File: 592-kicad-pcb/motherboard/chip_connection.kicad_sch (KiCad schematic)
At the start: 28 parts, among them J3 DF40C-40DP-0.4V(51), J4 DF40C-40DP-0.4V(51), J5 Conn_01x16, J6 Conn_01x16, J7 Conn_01x16

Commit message: finalize termination
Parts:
- removed J5, J6, J7: Conn_01x16, Connector_PinHeader_2.54mm:PinHeader_1x16_P2.54mm_Vertical, symbol Connector_Generic:Conn_01x16
- removed R10, R14, R15, R16, R17, R19, R20, R8, R9: 10k, Resistor_SMD:R_0603_1608Metric, symbol Device:R_Small
- removed R74, R75, R76, R77: 0, Resistor_SMD:R_0402_1005Metric, symbol Device:R_Small
- added C50: 100n, Capacitor_SMD:C_0402_1005Metric, symbol Device:C_Small
- added C51, C52: 100p, symbol Device:C_Small
- added J31: Conn_02x01, Connector_PinHeader_1.27mm:PinHeader_1x02_P1.27mm_Vertical, symbol Connector_Generic:Conn_02x01
- added R100, R101, R102, R103, R87, R88, R89: 0, symbol Device:R_Small
- added R73, R90, R91: 10k, Resistor_SMD:R_0603_1608Metric, symbol Device:R_Small
- added R84, R86: 68, symbol Device:R_Small
- added U29, U30, U31, U32: 74CBTLV3257, symbol 74xx:74CBTLV3257
- R11: now not fitted
- R18: footprint Resistor_SMD:R_0603_1608Metric -> Resistor_SMD:R_0402_1005Metric; LCSC C25804 -> C25744
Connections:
- net +3V3: now also R73.1, R90.1, U29.16 (VCC), U30.16 (VCC), U31.16 (VCC), U32.16 (VCC)
- net GND: now also C50.2, C51.2, C52.2, J31.1 (Pin_1), R91.2, U29.8 (GND), U30.8 (GND), U31.8 (GND), U32.8 (GND)
- net GPIO_MGMT_debug: now also U32.2
- net MGMT_CSB: now also U31.5
- net MGMT_SCK: now also U31.2
- net MGMT_SDI: now also U31.11
- net MGMT_SDO: now also U31.14
- net MGMT_flash2_csb: now also U30.2
- net MGMT_flash2_io0: now also U29.11
- net MGMT_flash2_io1: now also U29.5
- net MGMT_flash2_sck: now also U29.14
- net MGMT_irq: now also U30.5
- net MGMT_irq2: now also U29.2
- net MGMT_ser_rx: now also U30.14
- net MGMT_ser_tx: now also U30.11
- net TCK_EXT: now also R84.1
- net ext_reset_dig: now also R11.2
- net gpio_0_0: now also U29.13
- net gpio_1_0: now also U29.10
- net i2c_0_scl: now also U29.3
- net i2c_0_sda: now also U29.6
- net jtag_TCK: now also R86.1, U32.3
- net jtag_TDI: now also U31.10
- net jtag_TDO: now also R87.2
- net jtag_TMS: now also U31.13; no longer R18.2
- net mprj_io_0: now also U32.4
- net mprj_io_10: now also U29.9
- net mprj_io_11: now also U29.7
- net mprj_io_12: now also U29.4
- net mprj_io_2: now also U31.9
- net mprj_io_3: now also U31.7
- net mprj_io_4: now also U31.4
- net mprj_io_5: now also U30.12
- net mprj_io_6: now also U30.9
- net mprj_io_7: now also U30.7
- net mprj_io_8: now also U30.4
- net mprj_io_9: now also U29.12
- net reset_io: now also R73.2, U30.3
- net resetb: now also R90.2, R91.1; no longer R11.2
- net spi_0_cs_0: now also U30.10
- net spi_0_dq_0: now also U30.13
- net spi_0_dq_1: now also U31.3
- net spi_0_sck: now also U30.6
- net spi_flash_0_dq_0: now also R103.2; no longer J4.15
- net spi_flash_0_dq_1: now also R102.2; no longer J4.13
- net spi_flash_0_dq_2: now also R101.2; no longer J4.11
- net spi_flash_0_dq_3: now also R100.2; no longer J4.9
- net tdo: now also R88.2; no longer J4.25
- net tdo2: now also R89.1; no longer J3.30
- new net: J4.11, R101.1
- new net: J4.13, R102.1
- new net: J4.15, R103.1
- new net: J4.25, R88.1
- new net: J4.9, R100.1
- new net: C51.1, R84.2
- new net: U29.15 (~{OE}), U30.15 (~{OE}), U31.15 (~{OE}), U32.15 (~{OE})
- new net: R87.1, U31.6
- new net: J3.30, R89.2
- new net: C52.1, R86.2
- new net GPIO_MGMT_enable: C50.1, J31.2 (Pin_2), R18.2, U29.1 (S), U30.1 (S), U31.1 (S), U32.1 (S)
- no-connect marks 63 -> 61
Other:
- note added: "clock termination on JTAG should be as close to source as possible"
- note added: "pull-up for i2c (from rck)"
- note removed: "configure STM GPIO to use PDN for TDO inputs"
- note removed: "conns adjacent to each other. use 2.54mm jumpers to select from chip"
- note removed: "for mgmt spi"
- note removed: "go to 4x mux chips idea: have a single jumper that's "management mode" that handles all sources of interest"
- note removed: "pd/pu as per ARM JTAG spec"
- note removed: "pull up on CSb to avoid tristate periph in"
- note removed: "pull-up for i2c"
- moved on the sheet: R12, R13

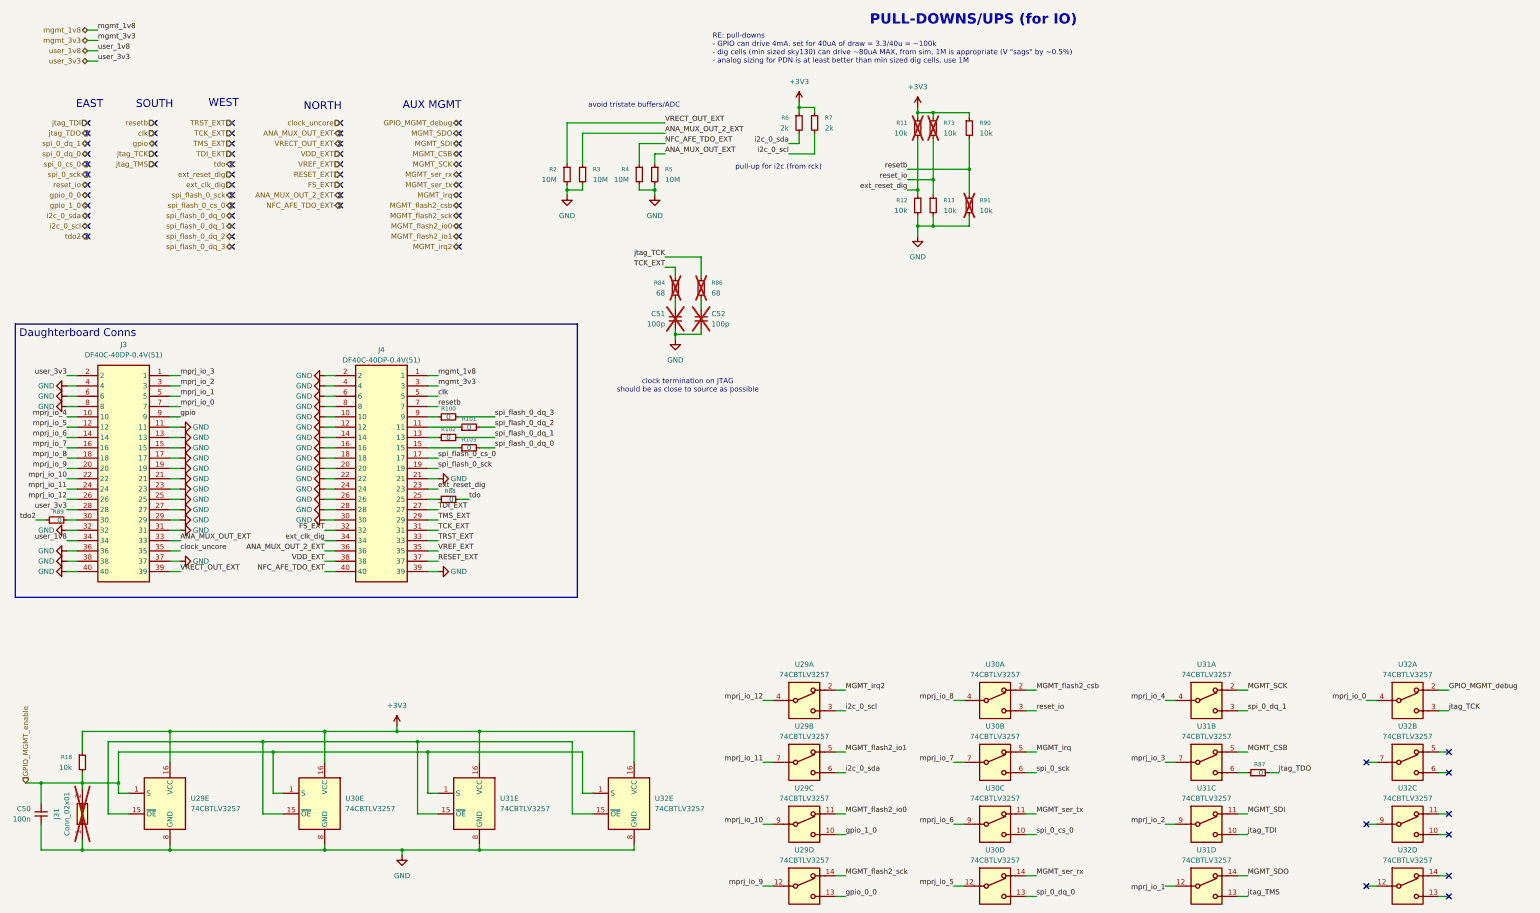
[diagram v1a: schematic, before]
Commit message: update jlcpcb part numbers
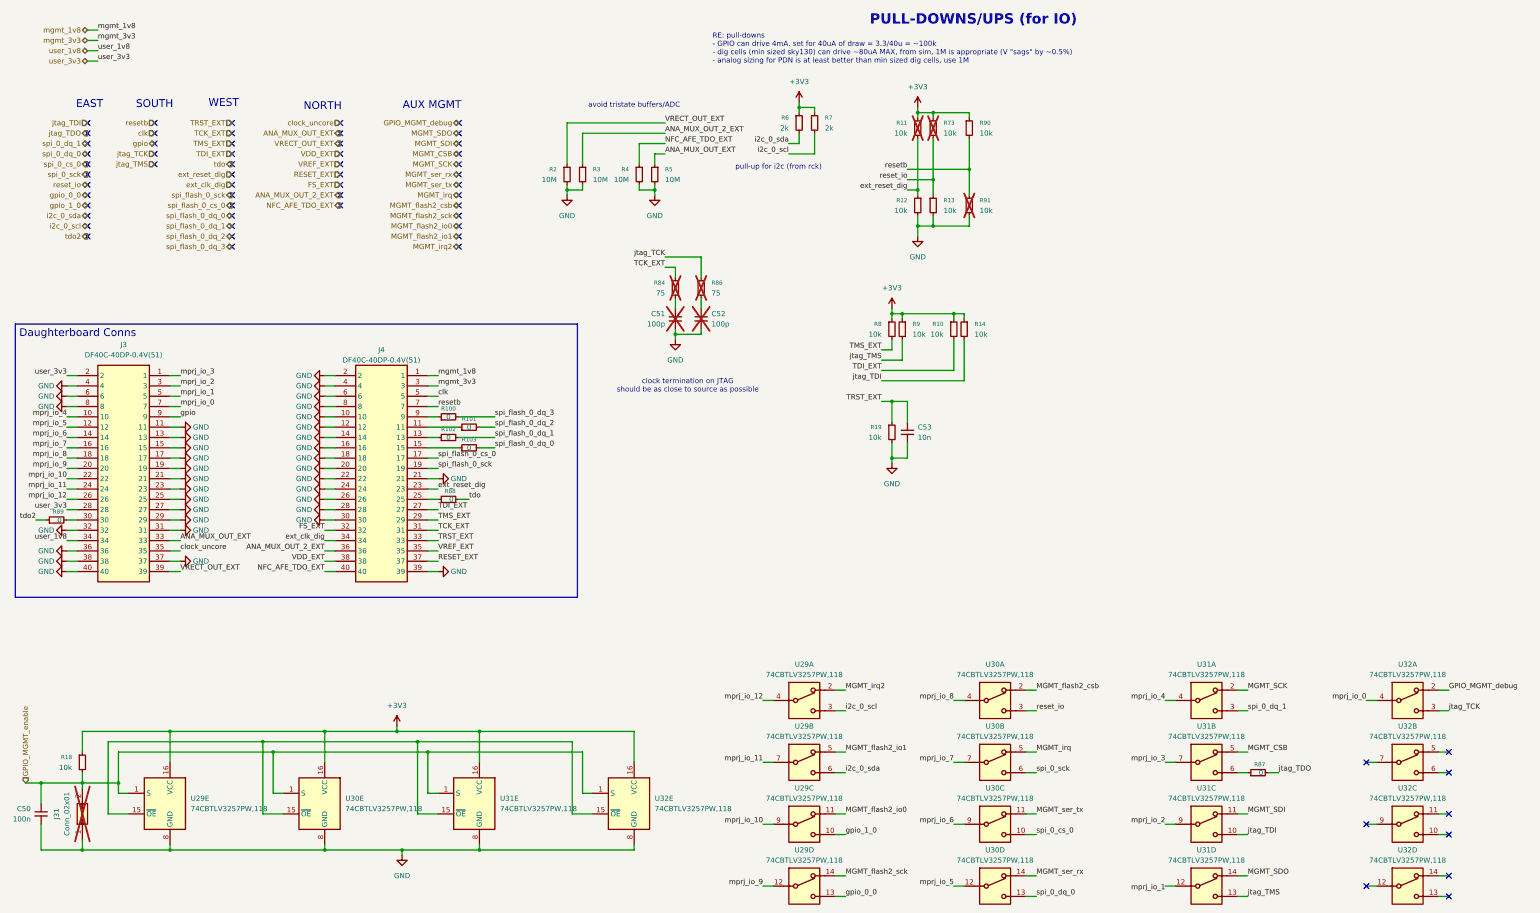
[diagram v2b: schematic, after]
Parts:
- added C53: 10n, Capacitor_SMD:C_0402_1005Metric, symbol Device:C_Small
- added R10, R14, R19, R8, R9: 10k, Resistor_SMD:R_0402_1005Metric, symbol Device:R_Small
- C51, C52: footprint (none) -> Capacitor_SMD:C_0402_1005Metric
- R100, R101, R102, R103, R87, R88, R89: footprint (none) -> Resistor_SMD:R_0402_1005Metric; LCSC (none) -> C17168
- R84, R86: value 68 -> 75; footprint (none) -> Resistor_SMD:R_0603_1608Metric; LCSC (none) -> C4275
- U29, U30, U31, U32: value 74CBTLV3257 -> 74CBTLV3257PW,118; footprint (none) -> Package_SO:TSSOP-16_4.4x5mm_P0.65mm; LCSC (none) -> C546455
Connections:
- net +3V3: now also R10.1, R14.1, R8.1, R9.1
- net GND: now also C53.2, R19.2
- net TDI_EXT: now also R10.2
- net TMS_EXT: now also R8.2
- net TRST_EXT: now also C53.1, R19.1
- net jtag_TDI: now also R14.2
- net jtag_TMS: now also R9.2

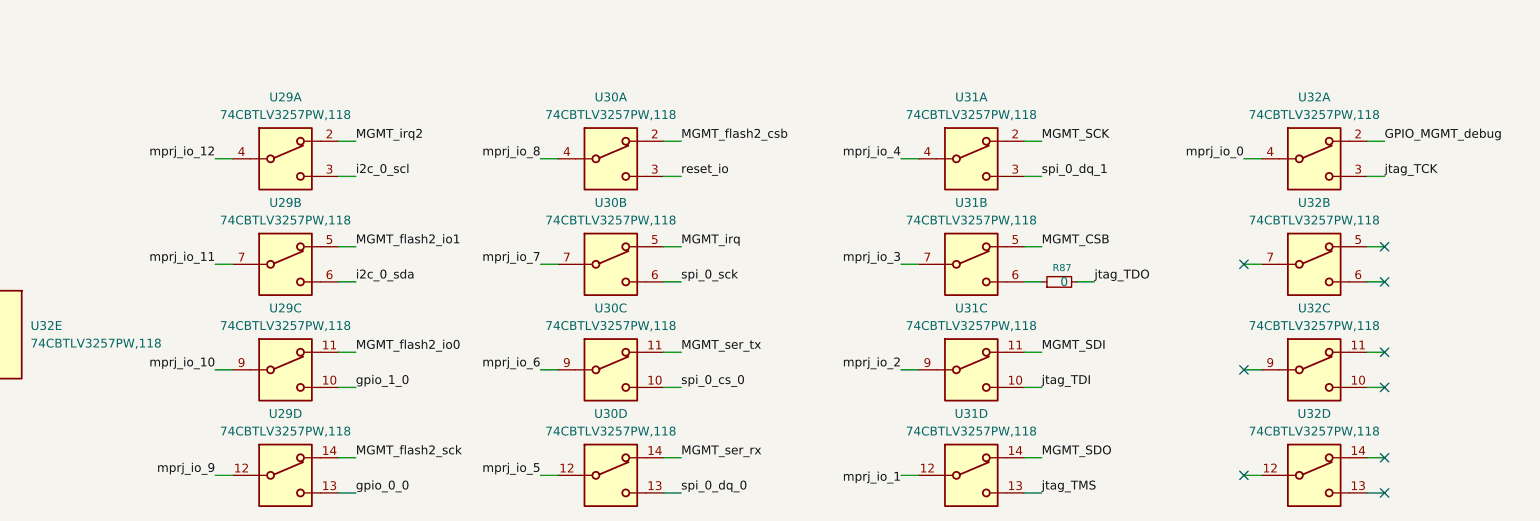
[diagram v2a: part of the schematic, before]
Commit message: core routing progress
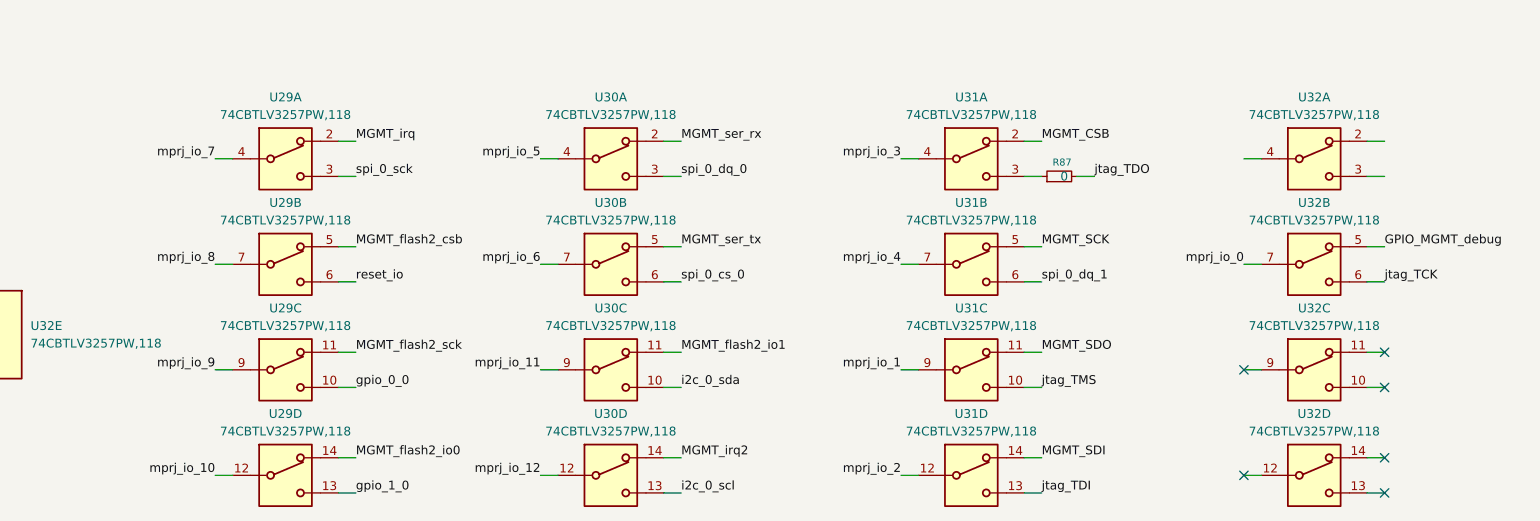
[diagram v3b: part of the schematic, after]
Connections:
- net GPIO_MGMT_debug: now also U32.5; no longer U32.2
- net MGMT_CSB: now also U31.2; no longer U31.5
- net MGMT_SCK: now also U31.5; no longer U31.2
- net MGMT_SDI: now also U31.14; no longer U31.11
- net MGMT_SDO: now also U31.11; no longer U31.14
- net MGMT_flash2_csb: now also U29.5; no longer U30.2
- net MGMT_flash2_io0: now also U29.14; no longer U29.11
- net MGMT_flash2_io1: now also U30.11; no longer U29.5
- net MGMT_flash2_sck: now also U29.11; no longer U29.14
- net MGMT_irq: now also U29.2; no longer U30.5
- net MGMT_irq2: now also U30.14; no longer U29.2
- net MGMT_ser_rx: now also U30.2; no longer U30.14
- net MGMT_ser_tx: now also U30.5; no longer U30.11
- net gpio_0_0: now also U29.10; no longer U29.13
- net gpio_1_0: now also U29.13; no longer U29.10
- net i2c_0_scl: now also U30.13; no longer U29.3
- net i2c_0_sda: now also U30.10; no longer U29.6
- net jtag_TCK: now also U32.6; no longer U32.3
- net jtag_TDI: now also U31.13; no longer U31.10
- net jtag_TMS: now also U31.10; no longer U31.13
- net mprj_io_0: now also U32.7; no longer U32.4
- net mprj_io_1: now also U31.9
- net mprj_io_10: now also U29.12; no longer U29.9
- net mprj_io_11: now also U30.9; no longer U29.7
- net mprj_io_12: now also U30.12; no longer U29.4
- net mprj_io_2: now also U31.12; no longer U31.9
- net mprj_io_3: now also U31.4; no longer U31.7
- net mprj_io_4: now also U31.7; no longer U31.4
- net mprj_io_5: now also U30.4; no longer U30.12
- net mprj_io_6: now also U30.7; no longer U30.9
- net mprj_io_7: now also U29.4; no longer U30.7
- net mprj_io_8: now also U29.7; no longer U30.4
- net mprj_io_9: now also U29.9; no longer U29.12
- net reset_io: now also U29.6; no longer U30.3
- net spi_0_cs_0: now also U30.6; no longer U30.10
- net spi_0_dq_0: now also U30.3; no longer U30.13
- net spi_0_dq_1: now also U31.6; no longer U31.3
- net spi_0_sck: now also U29.3; no longer U30.6
- net at R87.1: now also U31.3; no longer U31.6
- no-connect marks 61 -> 58
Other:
- moved on the sheet: R87
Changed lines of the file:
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@@
 	)
 	(no_connect
-		(at 356.87 200.66)
-	)
-	(no_connect
 		(at 104.14 55.88)
 	)
@@
 	)
 	(no_connect
-		(at 377.19 198.12)
-	)
-	(no_connect
 		(at 133.35 48.26)
 	)
@@
 	)
 	(no_connect
-		(at 377.19 203.2)
-	)
-	(no_connect
 		(at 41.91 71.12)
 	)
@@
 	(wire
 		(pts
-			(xy 332.74 203.2) (xy 335.28 203.2)
+			(xy 332.74 187.96) (xy 335.28 187.96)
 		)
 		(stroke
@@
 	)
 	(label "mprj_io_0"
-		(at 356.87 185.42 180)
+		(at 356.87 200.66 180)
 		(effects
 			(font
@@
 	)
 	(label "mprj_io_12"
-		(at 208.28 185.42 180)
+		(at 255.27 231.14 180)
 		(effects
 			(font
@@
 	)
 	(label "MGMT_irq2"
-		(at 228.6 182.88 0)
+		(at 275.59 228.6 0)
 		(effects
 			(font
@@
 	)
 	(label "MGMT_SDI"
-		(at 327.66 213.36 0)
+		(at 327.66 228.6 0)
 		(effects
 			(font
@@
 	)
 	(label "spi_0_sck"
-		(at 275.59 203.2 0)
+		(at 228.6 187.96 0)
 		(effects
 			(font
@@
 	)
 	(label "MGMT_flash2_csb"
-		(at 275.59 182.88 0)
+		(at 228.6 198.12 0)
 		(effects
 			(font
@@
 	)
 	(label "mprj_io_4"
-		(at 307.34 185.42 180)
+		(at 307.34 200.66 180)
 		(effects
 			(font
@@
 	)
 	(label "mprj_io_8"
-		(at 255.27 185.42 180)
+		(at 208.28 200.66 180)
 		(effects
 			(font
@@
 	)
 	(label "gpio_0_0"
-		(at 228.6 233.68 0)
+		(at 228.6 218.44 0)
 		(effects
 			(font
@@
 	)
 	(label "gpio_1_0"
-		(at 228.6 218.44 0)
+		(at 228.6 233.68 0)
 		(effects
 			(font
@@
 	)
 	(label "mprj_io_10"
-		(at 208.28 215.9 180)
+		(at 208.28 231.14 180)
 		(effects
 			(font
@@
 	)
 	(label "mprj_io_5"
-		(at 255.27 231.14 180)
+		(at 255.27 185.42 180)
 		(effects
 			(font
@@
 	)
 	(label "mprj_io_7"
-		(at 255.27 200.66 180)
+		(at 208.28 185.42 180)
 		(effects
 			(font
@@
 	)
 	(label "mprj_io_1"
-		(at 307.34 232.41 180)
+		(at 307.34 215.9 180)
 		(effects
 			(font
@@
 	)
 	(label "mprj_io_11"
-		(at 208.28 200.66 180)
+		(at 255.27 215.9 180)
 		(effects
 			(font
@@
 	)
 	(label "jtag_TCK"
-		(at 377.19 187.96 0)
+		(at 377.19 203.2 0)
 		(effects
 			(font
@@
 	)
 	(label "MGMT_SDO"
-		(at 327.66 228.6 0)
+		(at 327.66 213.36 0)
 		(effects
 			(font
@@
 	)
 	(label "MGMT_flash2_sck"
-		(at 228.6 228.6 0)
+		(at 228.6 213.36 0)
 		(effects
 			(font
@@
 	)
 	(label "i2c_0_sda"
-		(at 228.6 203.2 0)
+		(at 275.59 218.44 0)
 		(effects
 			(font
@@
 	)
 	(label "MGMT_flash2_io1"
-		(at 228.6 198.12 0)
+		(at 275.59 213.36 0)
 		(effects
 			(font
@@
 	)
 	(label "GPIO_MGMT_debug"
-		(at 377.19 182.88 0)
+		(at 377.19 198.12 0)
 		(effects
 			(font
@@
 	)
 	(label "MGMT_flash2_io0"
-		(at 228.6 213.36 0)
+		(at 228.6 228.6 0)
 		(effects
 			(font
@@
 	)
 	(label "MGMT_CSB"
-		(at 327.66 198.12 0)
+		(at 327.66 182.88 0)
 		(effects
 			(font
@@
 	)
 	(label "reset_io"
-		(at 275.59 187.96 0)
+		(at 228.6 203.2 0)
 		(effects
 			(font
@@
 	)
 	(label "mprj_io_3"
-		(at 307.34 200.66 180)
+		(at 307.34 185.42 180)
 		(effects
 			(font
@@
 	)
 	(label "jtag_TDI"
-		(at 327.66 218.44 0)
+		(at 327.66 233.68 0)
 		(effects
 			(font
@@
 	)
 	(label "MGMT_SCK"
-		(at 327.66 182.88 0)
+		(at 327.66 198.12 0)
 		(effects
 			(font
@@
 	)
 	(label "i2c_0_scl"
-		(at 228.6 187.96 0)
+		(at 275.59 233.68 0)
 		(effects
 			(font
@@
 	)
 	(label "mprj_io_9"
-		(at 208.28 231.14 180)
+		(at 208.28 215.9 180)
 		(effects
 			(font
@@
 	)
 	(label "jtag_TDO"
-		(at 335.28 203.2 0)
+		(at 335.28 187.96 0)
 		(effects
 			(font
@@
 	)
 	(label "MGMT_ser_rx"
-		(at 275.59 228.6 0)
+		(at 275.59 182.88 0)
 		(effects
 			(font
@@
 	)
 	(label "MGMT_ser_tx"
-		(at 275.59 213.36 0)
+		(at 275.59 198.12 0)
 		(effects
 			(font
@@
 	)
 	(label "spi_0_dq_1"
-		(at 327.66 187.96 0)
+		(at 327.66 203.2 0)
 		(effects
 			(font
@@
 	)
 	(label "spi_0_dq_0"
-		(at 275.59 233.68 0)
+		(at 275.59 187.96 0)
 		(effects
 			(font
@@
 	)
 	(label "spi_0_cs_0"
-		(at 275.59 218.44 0)
+		(at 275.59 203.2 0)
 		(effects
 			(font
@@
 	)
 	(label "jtag_TMS"
-		(at 327.66 233.68 0)
+		(at 327.66 218.44 0)
 		(effects
 			(font
@@
 	)
 	(label "MGMT_irq"
-		(at 275.59 198.12 0)
+		(at 228.6 182.88 0)
 		(effects
 			(font
@@
 	)
 	(label "mprj_io_6"
-		(at 255.27 215.9 180)
+		(at 255.27 200.66 180)
 		(effects
 			(font
@@
 	)
 	(label "mprj_io_2"
-		(at 307.34 215.9 180)
+		(at 307.34 231.14 180)
 		(effects
 			(font
@@
 	(symbol
 		(lib_id "Device:R_Small")
-		(at 330.2 203.2 90)
+		(at 330.2 187.96 90)
 		(unit 1)
 		(exclude_from_sim no)
@@
 		(dnp no)
 		(property "Reference" "R87"
-			(at 331.978 201.168 90)
+			(at 331.978 185.928 90)
 			(effects
 				(font
@@
 		)
 		(property "Value" "0"
-			(at 331.47 203.2 90)
+			(at 331.47 187.96 90)
 			(effects
 				(font
@@
 		)
 		(property "Footprint" "Resistor_SMD:R_0402_1005Metric"
-			(at 330.2 203.2 0)
+			(at 330.2 187.96 0)
 			(effects
 				(font
@@
 		)
 		(property "Datasheet" "~"
-			(at 330.2 203.2 0)
+			(at 330.2 187.96 0)
 			(effects
 				(font
@@
 		)
 		(property "Description" "Resistor, small symbol"
-			(at 330.2 203.2 0)
+			(at 330.2 187.96 0)
 			(effects
 				(font
@@
 		)
 		(property "LCSC" "C17168"
-			(at 330.2 203.2 90)
+			(at 330.2 187.96 90)
 			(effects
 				(font
